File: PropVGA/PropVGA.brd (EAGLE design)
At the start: 33.3 x 31.7 mm, 10 parts

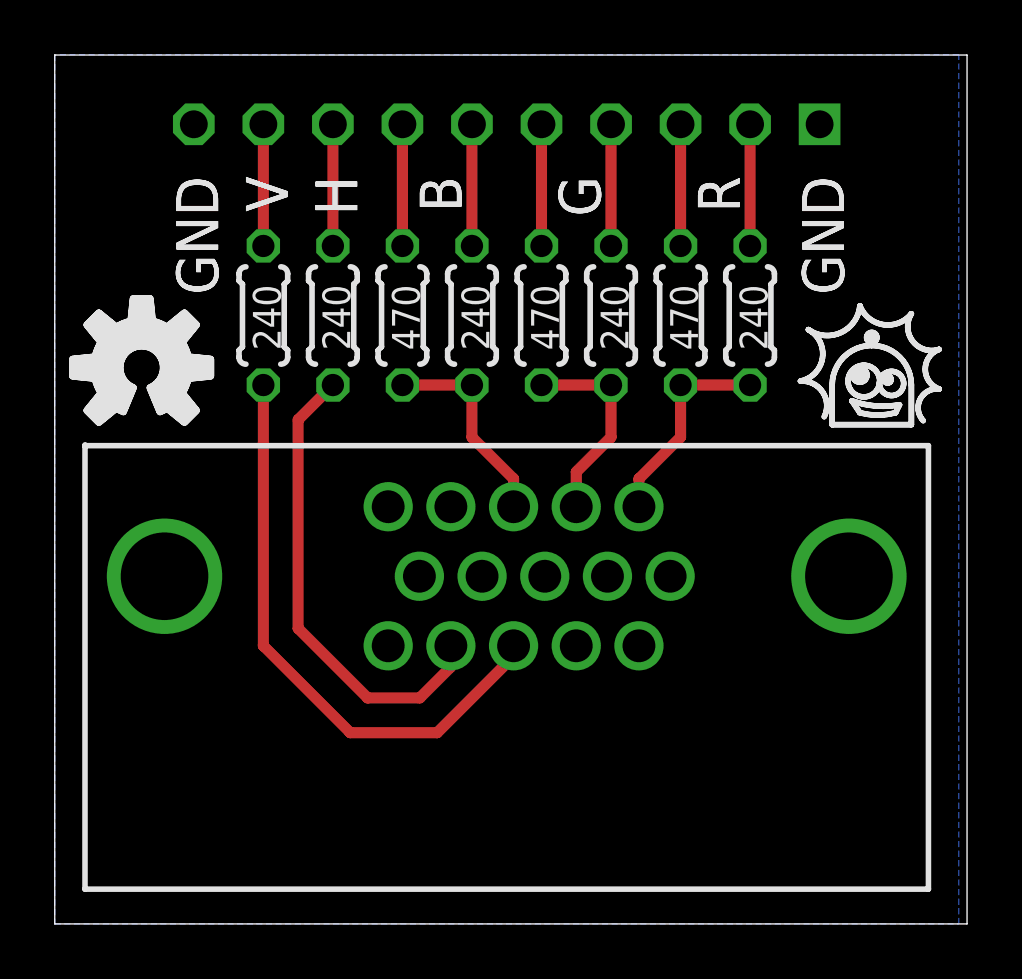
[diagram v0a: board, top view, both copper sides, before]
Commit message: Corrected HSYNC / VSYNC connections
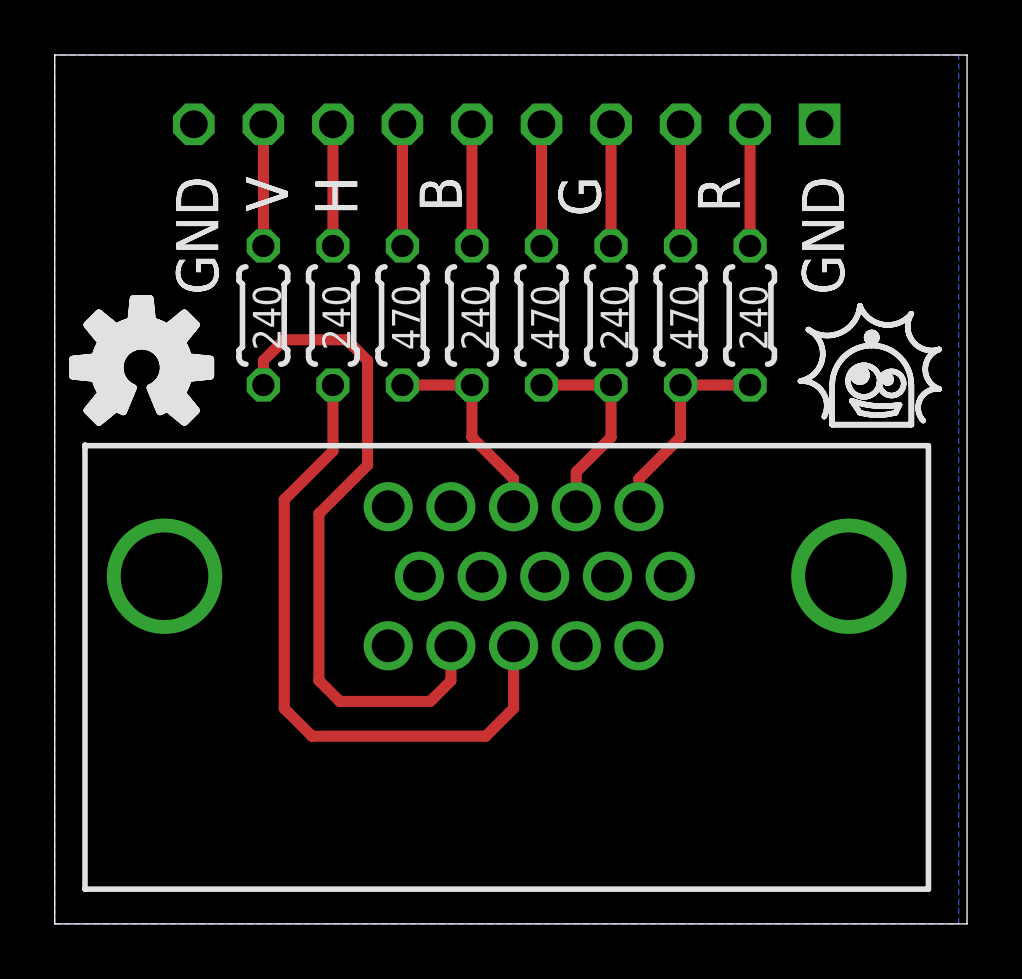
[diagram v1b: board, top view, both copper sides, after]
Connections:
- net H: now also JP2.P13; no longer JP2.P14
- net V: now also JP2.P14; no longer JP2.P13
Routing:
- net H: track 17.3 -> 24.1 mm
- net V: track 21.5 -> 24.5 mm
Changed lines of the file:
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@@
 <setting verticaltext="up"/>
 </settings>
-<grid distance="0.05" unitdist="inch" unit="inch" style="lines" multiple="1" display="no" altdistance="0.025" altunitdist="inch" altunit="inch"/>
+<grid distance="0.01" unitdist="inch" unit="inch" style="lines" multiple="1" display="no" altdistance="0.025" altunitdist="inch" altunit="inch"/>
 <layers>
 <layer number="1" name="Top" color="4" fill="1" visible="yes" active="yes"/>
@@
 <signal name="V">
 <contactref element="R1" pad="1"/>
-<contactref element="JP2" pad="P13"/>
-<wire x1="16.76" y1="10.16" x2="16.76" y2="9.775" width="0.4064" layer="1"/>
-<wire x1="16.76" y1="9.775" x2="13.97" y2="6.985" width="0.4064" layer="1"/>
-<wire x1="13.97" y1="6.985" x2="10.795" y2="6.985" width="0.4064" layer="1"/>
-<wire x1="10.795" y1="6.985" x2="7.62" y2="10.16" width="0.4064" layer="1"/>
-<wire x1="7.62" y1="10.16" x2="7.62" y2="19.685" width="0.4064" layer="1"/>
+<contactref element="JP2" pad="P14"/>
+<wire x1="14.47" y1="10.16" x2="14.47" y2="8.882" width="0.4064" layer="1"/>
+<wire x1="14.47" y1="8.882" x2="13.716" y2="8.128" width="0.4064" layer="1"/>
+<wire x1="13.716" y1="8.128" x2="10.414" y2="8.128" width="0.4064" layer="1"/>
+<wire x1="10.414" y1="8.128" x2="9.652" y2="8.89" width="0.4064" layer="1"/>
+<wire x1="9.652" y1="8.89" x2="9.652" y2="14.986" width="0.4064" layer="1"/>
+<wire x1="9.652" y1="14.986" x2="11.43" y2="16.764" width="0.4064" layer="1"/>
+<wire x1="11.43" y1="16.764" x2="11.43" y2="20.574" width="0.4064" layer="1"/>
+<wire x1="11.43" y1="20.574" x2="10.668" y2="21.336" width="0.4064" layer="1"/>
+<wire x1="10.668" y1="21.336" x2="8.382" y2="21.336" width="0.4064" layer="1"/>
+<wire x1="8.382" y1="21.336" x2="7.62" y2="20.574" width="0.4064" layer="1"/>
+<wire x1="7.62" y1="20.574" x2="7.62" y2="19.685" width="0.4064" layer="1"/>
 </signal>
 <signal name="H">
 <contactref element="R2" pad="1"/>
-<contactref element="JP2" pad="P14"/>
-<wire x1="14.47" y1="10.16" x2="14.47" y2="9.39" width="0.4064" layer="1"/>
-<wire x1="14.47" y1="9.39" x2="13.335" y2="8.255" width="0.4064" layer="1"/>
-<wire x1="13.335" y1="8.255" x2="11.43" y2="8.255" width="0.4064" layer="1"/>
-<wire x1="11.43" y1="8.255" x2="8.89" y2="10.795" width="0.4064" layer="1"/>
-<wire x1="8.89" y1="10.795" x2="8.89" y2="18.415" width="0.4064" layer="1"/>
-<wire x1="8.89" y1="18.415" x2="10.16" y2="19.685" width="0.4064" layer="1"/>
+<contactref element="JP2" pad="P13"/>
+<wire x1="10.16" y1="19.685" x2="10.16" y2="17.272" width="0.4064" layer="1"/>
+<wire x1="10.16" y1="17.272" x2="8.382" y2="15.494" width="0.4064" layer="1"/>
+<wire x1="8.382" y1="15.494" x2="8.382" y2="7.874" width="0.4064" layer="1"/>
+<wire x1="8.382" y1="7.874" x2="9.398" y2="6.858" width="0.4064" layer="1"/>
+<wire x1="9.398" y1="6.858" x2="15.748" y2="6.858" width="0.4064" layer="1"/>
+<wire x1="15.748" y1="6.858" x2="16.764" y2="7.874" width="0.4064" layer="1"/>
+<wire x1="16.764" y1="7.874" x2="16.764" y2="10.156" width="0.4064" layer="1"/>
+<wire x1="16.764" y1="10.156" x2="16.76" y2="10.16" width="0.4064" layer="1"/>
 </signal>
 <signal name="B">

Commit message: Fixes to PropVGA, microSD,
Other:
- board size 33.3 x 31.7 mm -> 33 x 31.5 mm
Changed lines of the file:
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@@
 <layer number="22" name="bPlace" color="7" fill="1" visible="no" active="yes"/>
 <layer number="23" name="tOrigins" color="15" fill="1" visible="yes" active="yes"/>
-<layer number="24" name="bOrigins" color="15" fill="1" visible="no" active="yes"/>
+<layer number="24" name="bOrigins" color="15" fill="1" visible="yes" active="yes"/>
 <layer number="25" name="tNames" color="7" fill="1" visible="yes" active="yes"/>
 <layer number="26" name="bNames" color="7" fill="1" visible="no" active="yes"/>
@@
 <board>
 <plain>
-<wire x1="0" y1="0" x2="33.325" y2="0" width="0" layer="20"/>
-<wire x1="33.325" y1="0" x2="33.325" y2="31.74" width="0" layer="20"/>
-<wire x1="33.325" y1="31.74" x2="0" y2="31.74" width="0" layer="20"/>
-<wire x1="0" y1="31.74" x2="0" y2="0" width="0" layer="20"/>
+<wire x1="0" y1="0" x2="33.02" y2="0" width="0" layer="20"/>
+<wire x1="33.02" y1="0" x2="33.02" y2="22.098" width="0" layer="20"/>
+<wire x1="33.02" y1="22.098" x2="30.226" y2="24.892" width="0" layer="20"/>
+<wire x1="30.226" y1="24.892" x2="30.226" y2="29.910371875" width="0" layer="20"/>
+<wire x1="30.226" y1="29.910371875" x2="28.640371875" y2="31.496" width="0" layer="20"/>
+<wire x1="28.640371875" y1="31.496" x2="4.379628125" y2="31.496" width="0" layer="20"/>
+<wire x1="4.379628125" y1="31.496" x2="2.794" y2="29.910371875" width="0" layer="20"/>
+<wire x1="2.794" y1="29.910371875" x2="2.794" y2="24.892" width="0" layer="20"/>
+<wire x1="2.794" y1="24.892" x2="0" y2="22.098" width="0" layer="20"/>
+<wire x1="0" y1="22.098" x2="0" y2="0" width="0" layer="20"/>
 <text x="27.305" y="27.305" size="1.524" layer="25" font="vector" ratio="10" rot="R270">GND</text>
 <text x="30.48" y="2.54" size="1.778" layer="26" font="vector" rot="MR0">bot-thoughts.com</text>
@@
 <wire x1="13.716" y1="8.128" x2="10.414" y2="8.128" width="0.4064" layer="1"/>
 <wire x1="10.414" y1="8.128" x2="9.652" y2="8.89" width="0.4064" layer="1"/>
-<wire x1="9.652" y1="8.89" x2="9.652" y2="14.986" width="0.4064" layer="1"/>
-<wire x1="9.652" y1="14.986" x2="11.43" y2="16.764" width="0.4064" layer="1"/>
-<wire x1="11.43" y1="16.764" x2="11.43" y2="20.574" width="0.4064" layer="1"/>
+<wire x1="9.652" y1="8.89" x2="9.652" y2="16.002" width="0.4064" layer="1"/>
+<wire x1="9.652" y1="16.002" x2="11.43" y2="17.78" width="0.4064" layer="1"/>
+<wire x1="11.43" y1="17.78" x2="11.43" y2="20.574" width="0.4064" layer="1"/>
 <wire x1="11.43" y1="20.574" x2="10.668" y2="21.336" width="0.4064" layer="1"/>
 <wire x1="10.668" y1="21.336" x2="8.382" y2="21.336" width="0.4064" layer="1"/>
@@
 <contactref element="R2" pad="1"/>
 <contactref element="JP2" pad="P13"/>
-<wire x1="10.16" y1="19.685" x2="10.16" y2="17.272" width="0.4064" layer="1"/>
-<wire x1="10.16" y1="17.272" x2="8.382" y2="15.494" width="0.4064" layer="1"/>
-<wire x1="8.382" y1="15.494" x2="8.382" y2="7.874" width="0.4064" layer="1"/>
+<wire x1="10.16" y1="19.685" x2="10.16" y2="18.288" width="0.4064" layer="1"/>
+<wire x1="10.16" y1="18.288" x2="8.382" y2="16.51" width="0.4064" layer="1"/>
+<wire x1="8.382" y1="16.51" x2="8.382" y2="7.874" width="0.4064" layer="1"/>
 <wire x1="8.382" y1="7.874" x2="9.398" y2="6.858" width="0.4064" layer="1"/>
 <wire x1="9.398" y1="6.858" x2="15.748" y2="6.858" width="0.4064" layer="1"/>
